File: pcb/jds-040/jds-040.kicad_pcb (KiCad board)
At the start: 2 copper layers, 18.1 x 21.5 mm, 8 parts, among them J1 USB_C_Receptacle_USB2.0, J2 Conn_01x12_MountingPin

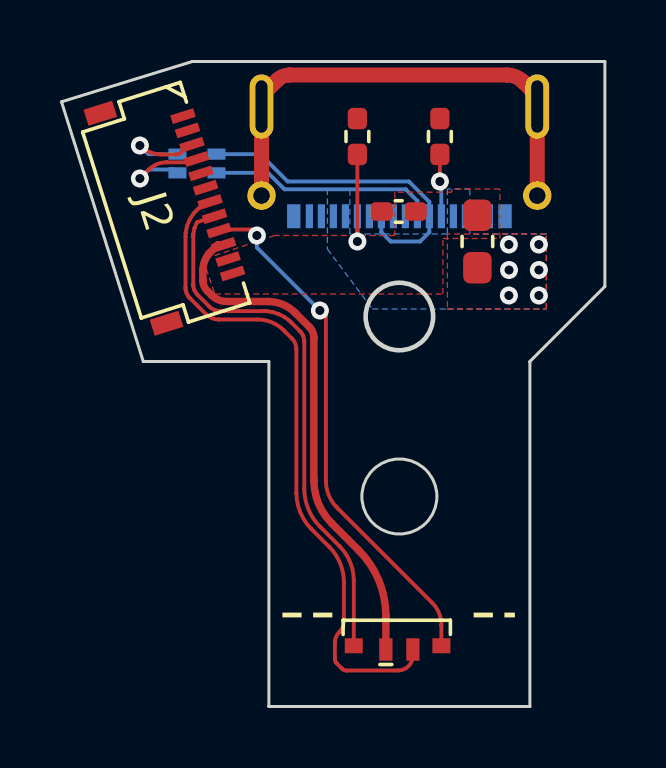
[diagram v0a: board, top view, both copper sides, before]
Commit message: Rounded all tracks, increased spaces in ground zone.
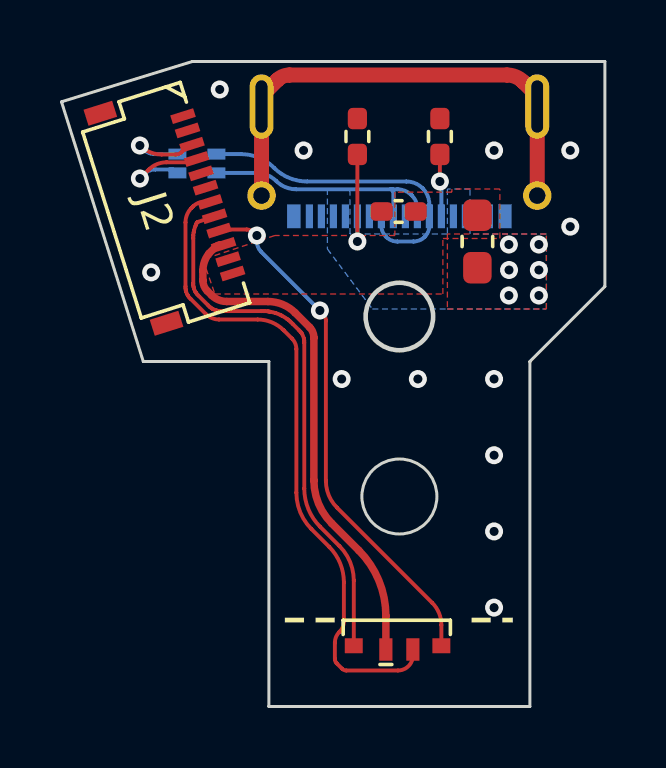
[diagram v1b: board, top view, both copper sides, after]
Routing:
- net /OD-: track 7.60 -> 8.43 mm
- net GND: vias 0 -> 12

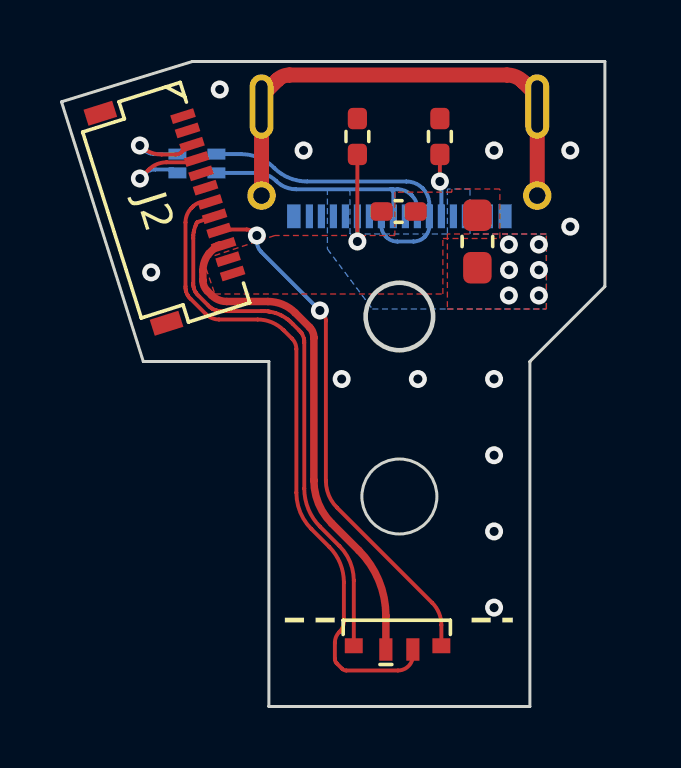
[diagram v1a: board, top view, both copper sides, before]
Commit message: Finished silkscreen, minor adjustments.
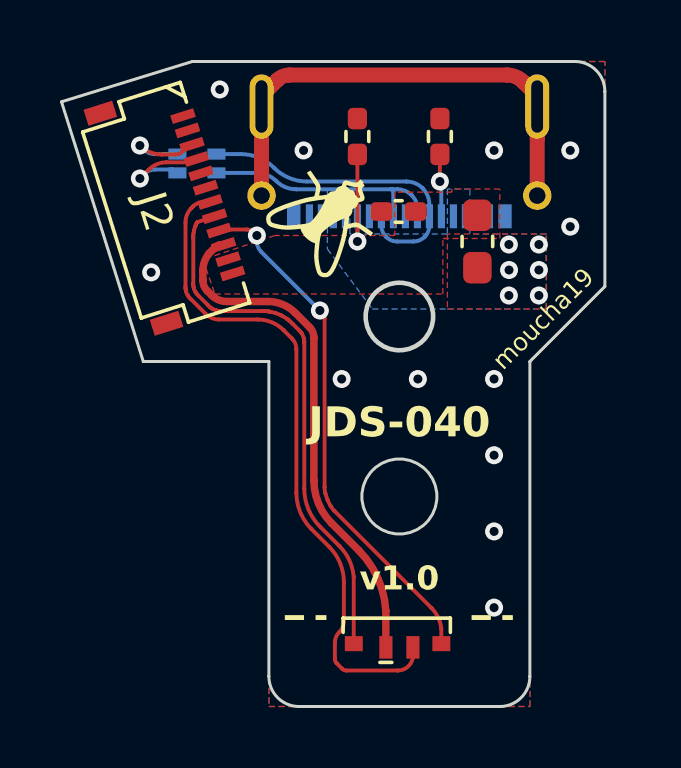
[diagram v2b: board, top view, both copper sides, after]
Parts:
- added REF**: Logo_Moucha_3x3mm_SilkScreen, Moucha_Graphics:Logo_Moucha_3x3mm_SilkScreen, F.Cu at (93.2, 95.2)
- C1: value 100nF -> 10nF
- moved D2 0.07 mm to (95.7, 109.5)
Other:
- outline, holes or cut-outs redrawn
- board text added: "JDS-040"
- board text added: "moucha19"
- board text added: "v1.0"

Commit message: Fixed DRC errors, cleaned tracks.
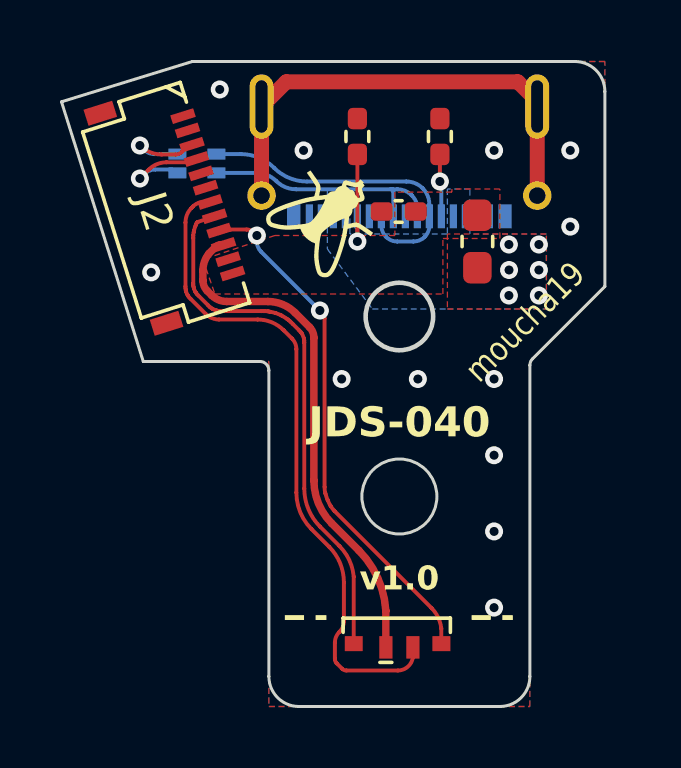
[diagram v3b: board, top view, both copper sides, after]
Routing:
- net /OD+: track 11.2 -> 10.3 mm
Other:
- outline, holes or cut-outs redrawn
- board text added: "JLCJLCJLCJLC"

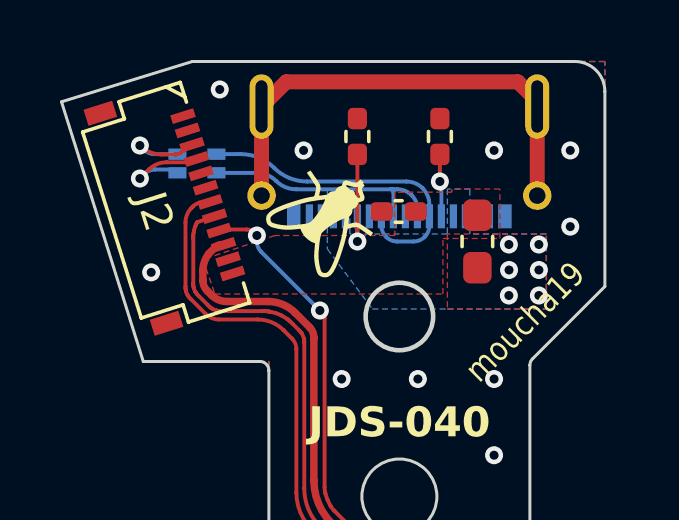
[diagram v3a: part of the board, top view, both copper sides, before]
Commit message: Increased thermal relief bridge width, minor fixes.
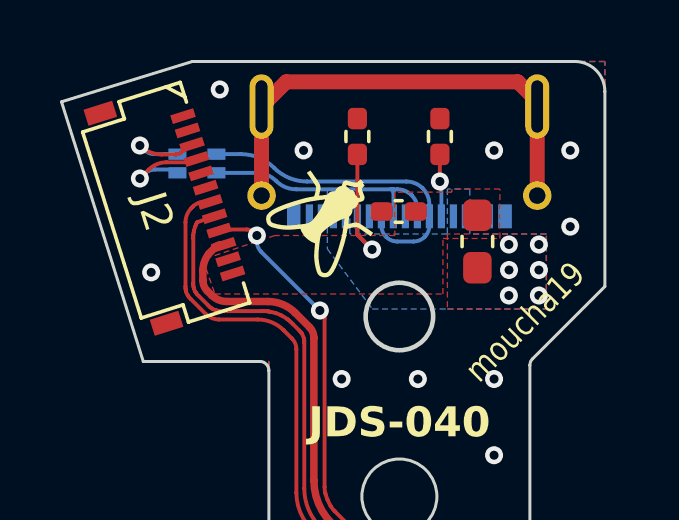
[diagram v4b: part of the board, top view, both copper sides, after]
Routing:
- net Net-(J1-CC1): track 3.74 -> 4.68 mm
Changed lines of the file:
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@@
     )
   )
-  (footprint "Moucha_Connectors:USBC_Receptacle_GT-USB-7025" (layer "B.Cu")
+  (footprint "Moucha_Connectors:USBC_Receptacle_GT-USB-7025" locked (layer "B.Cu")
     (at 95.65 91.5)
     (descr "Short USB Type-C receptacle for USB 2.0 and PD")
@@
     (property "ki_description" "USB 2.0-only Type-C Receptacle connector")
     (property "ki_keywords" "usb universal serial bus type-C USB2.0")
-    (attr smd)
+    (attr through_hole)
     (fp_text reference "J1" (at 0 0 180) (layer "B.SilkS")
         (effects (font (size 1 1) (thickness 0.15)) (justify mirror))
@@
     (fp_line (start 4.595 3.65) (end 4.595 -2.54)
       (stroke (width 0.1) (type solid)) (layer "B.Fab"))
-    (pad "A1" smd rect (at -3.52 3.66) (size 0.45 0.8) (layers "B.Cu" "B.Paste" "B.Mask")
-      (net 2 "GND") (pinfunction "GND") (pintype "passive"))
-    (pad "A1" smd rect (at -3 3.66) (size 0.24 0.8) (layers "B.Cu" "B.Paste" "B.Mask")
-      (net 2 "GND") (pinfunction "GND") (pintype "passive"))
-    (pad "A4" smd rect (at -2.2 3.66) (size 0.24 0.8) (layers "B.Cu" "B.Paste" "B.Mask")
+    (pad "A1" smd rect locked (at -3.52 3.66) (size 0.45 0.8) (layers "B.Cu" "B.Paste" "B.Mask")
+      (net 2 "GND") (pinfunction "GND") (pintype "passive"))
+    (pad "A1" smd rect locked (at -3 3.66) (size 0.24 0.8) (layers "B.Cu" "B.Paste" "B.Mask")
+      (net 2 "GND") (pinfunction "GND") (pintype "passive"))
+    (pad "A4" smd rect locked (at -2.2 3.66) (size 0.24 0.8) (layers "B.Cu" "B.Paste" "B.Mask")
       (net 1 "VBUS") (pinfunction "VBUS") (pintype "passive"))
-    (pad "A5" smd rect (at -1.4 3.66) (size 0.24 0.8) (layers "B.Cu" "B.Paste" "B.Mask")
+    (pad "A5" smd rect locked (at -1.4 3.66) (size 0.24 0.8) (layers "B.Cu" "B.Paste" "B.Mask")
       (net 12 "Net-(J1-CC1)") (pinfunction "CC1") (pintype "bidirectional"))
-    (pad "A6" smd rect (at -0.6 3.66) (size 0.24 0.8) (layers "B.Cu" "B.Paste" "B.Mask")
+    (pad "A6" smd rect locked (at -0.6 3.66) (size 0.24 0.8) (layers "B.Cu" "B.Paste" "B.Mask")
       (net 10 "/OD+") (pinfunction "D+") (pintype "bidirectional"))
-    (pad "A7" smd rect (at -0.2 3.66) (size 0.24 0.8) (layers "B.Cu" "B.Paste" "B.Mask")
+    (pad "A7" smd rect locked (at -0.2 3.66) (size 0.24 0.8) (layers "B.Cu" "B.Paste" "B.Mask")
       (net 8 "/OD-") (pinfunction "D-") (pintype "bidirectional"))
-    (pad "A8" smd rect (at 0.2 3.66) (size 0.24 0.8) (layers "B.Cu" "B.Paste" "B.Mask")
+    (pad "A8" smd rect locked (at 0.2 3.66) (size 0.24 0.8) (layers "B.Cu" "B.Paste" "B.Mask")
       (net 13 "unconnected-(J1-SBU1-PadA8)") (pinfunction "SBU1") (pintype "bidirectional+no_connect"))
-    (pad "A9" smd rect (at 1.8 3.66) (size 0.24 0.8) (layers "B.Cu" "B.Paste" "B.Mask")
+    (pad "A9" smd rect locked (at 1.8 3.66) (size 0.24 0.8) (layers "B.Cu" "B.Paste" "B.Mask")
       (net 1 "VBUS") (pinfunction "VBUS") (pintype "passive"))
-    (pad "A12" smd rect (at 2.6 3.66) (size 0.24 0.8) (layers "B.Cu" "B.Paste" "B.Mask")
-      (net 2 "GND") (pinfunction "GND") (pintype "passive"))
-    (pad "B1" smd rect (at 3 3.66) (size 0.24 0.8) (layers "B.Cu" "B.Paste" "B.Mask")
-      (net 2 "GND") (pinfunction "GND") (pintype "passive"))
-    (pad "B1" smd rect (at 3.52 3.66) (size 0.45 0.8) (layers "B.Cu" "B.Paste" "B.Mask")
-      (net 2 "GND") (pinfunction "GND") (pintype "passive"))
-    (pad "B4" smd rect (at 2.2 3.66) (size 0.24 0.8) (layers "B.Cu" "B.Paste" "B.Mask")
+    (pad "A12" smd rect locked (at 2.6 3.66) (size 0.24 0.8) (layers "B.Cu" "B.Paste" "B.Mask")
+      (net 2 "GND") (pinfunction "GND") (pintype "passive"))
+    (pad "B1" smd rect locked (at 3 3.66) (size 0.24 0.8) (layers "B.Cu" "B.Paste" "B.Mask")
+      (net 2 "GND") (pinfunction "GND") (pintype "passive"))
+    (pad "B1" smd rect locked (at 3.52 3.66) (size 0.45 0.8) (layers "B.Cu" "B.Paste" "B.Mask")
+      (net 2 "GND") (pinfunction "GND") (pintype "passive"))
+    (pad "B4" smd rect locked (at 2.2 3.66) (size 0.24 0.8) (layers "B.Cu" "B.Paste" "B.Mask")
       (net 1 "VBUS") (pinfunction "VBUS") (pintype "passive"))
-    (pad "B5" smd rect (at 1.4 3.66) (size 0.24 0.8) (layers "B.Cu" "B.Paste" "B.Mask")
+    (pad "B5" smd rect locked (at 1.4 3.66) (size 0.24 0.8) (layers "B.Cu" "B.Paste" "B.Mask")
       (net 14 "Net-(J1-CC2)") (pinfunction "CC2") (pintype "bidirectional"))
-    (pad "B6" smd rect (at 1 3.66) (size 0.24 0.8) (layers "B.Cu" "B.Paste" "B.Mask")
+    (pad "B6" smd rect locked (at 1 3.66) (size 0.24 0.8) (layers "B.Cu" "B.Paste" "B.Mask")
       (net 10 "/OD+") (pinfunction "D+") (pintype "bidirectional"))
-    (pad "B7" smd rect (at 0.6 3.66) (size 0.24 0.8) (layers "B.Cu" "B.Paste" "B.Mask")
+    (pad "B7" smd rect locked (at 0.6 3.66) (size 0.24 0.8) (layers "B.Cu" "B.Paste" "B.Mask")
       (net 8 "/OD-") (pinfunction "D-") (pintype "bidirectional"))
-    (pad "B8" smd rect (at -1 3.66) (size 0.24 0.8) (layers "B.Cu" "B.Paste" "B.Mask")
+    (pad "B8" smd rect locked (at -1 3.66) (size 0.24 0.8) (layers "B.Cu" "B.Paste" "B.Mask")
       (net 15 "unconnected-(J1-SBU2-PadB8)") (pinfunction "SBU2") (pintype "bidirectional+no_connect"))
-    (pad "B9" smd rect (at -1.8 3.66) (size 0.24 0.8) (layers "B.Cu" "B.Paste" "B.Mask")
+    (pad "B9" smd rect locked (at -1.8 3.66) (size 0.24 0.8) (layers "B.Cu" "B.Paste" "B.Mask")
       (net 1 "VBUS") (pinfunction "VBUS") (pintype "passive"))
-    (pad "B12" smd rect (at -2.6 3.66) (size 0.24 0.8) (layers "B.Cu" "B.Paste" "B.Mask")
-      (net 2 "GND") (pinfunction "GND") (pintype "passive"))
-    (pad "S1" thru_hole oval (at -4.595 0) (size 0.8 2.15) (drill oval 0.4 1.75) (layers "*.Cu" "*.Mask")
+    (pad "B12" smd rect locked (at -2.6 3.66) (size 0.24 0.8) (layers "B.Cu" "B.Paste" "B.Mask")
+      (net 2 "GND") (pinfunction "GND") (pintype "passive"))
+    (pad "S1" thru_hole oval locked (at -4.595 0) (size 0.8 2.15) (drill oval 0.4 1.75) (layers "*.Cu" "*.Mask")
       (net 16 "/SHIELD") (pinfunction "SHIELD") (pintype "passive"))
-    (pad "S1" thru_hole circle (at -4.595 2.97) (size 0.95 0.95) (drill 0.55) (layers "*.Cu" "*.Mask")
+    (pad "S1" thru_hole circle locked (at -4.595 2.97) (size 0.95 0.95) (drill 0.55) (layers "*.Cu" "*.Mask")
       (net 16 "/SHIELD") (pinfunction "SHIELD") (pintype "passive"))
-    (pad "S1" thru_hole oval (at 4.595 0) (size 0.8 2.15) (drill oval 0.4 1.75) (layers "*.Cu" "*.Mask")
+    (pad "S1" thru_hole oval locked (at 4.595 0) (size 0.8 2.15) (drill oval 0.4 1.75) (layers "*.Cu" "*.Mask")
       (net 16 "/SHIELD") (pinfunction "SHIELD") (pintype "passive"))
-    (pad "S1" thru_hole circle (at 4.595 2.97) (size 0.95 0.95) (drill 0.55) (layers "*.Cu" "*.Mask")
+    (pad "S1" thru_hole circle locked (at 4.595 2.97) (size 0.95 0.95) (drill 0.55) (layers "*.Cu" "*.Mask")
       (net 16 "/SHIELD") (pinfunction "SHIELD") (pintype "passive"))
     (model "${MOUCHA_LIB}/Moucha.3dshapes/USBC_Receptacle_TYPE-C-31-M-12.step"
@@
   (segment (start 87 92.8) (end 87.14375 92.94375) (width 0.13) (layer "B.Cu") (net 11))
   (arc (start 87.490793 93.0875) (mid 87.302974 93.05014) (end 87.14375 92.94375) (width 0.13) (layer "B.Cu") (net 11))
-  (segment (start 94.25 96) (end 94.25 93.0975) (width 0.13) (layer "F.Cu") (net 12))
-  (via (at 94.25 96) (size 0.6) (drill 0.3) (layers "F.Cu" "B.Cu") (net 12))
-  (segment (start 94.25 96) (end 94.25 95.16) (width 0.13) (layer "B.Cu") (net 12))
+  (segment (start 94.25 95.774) (end 94.25 93.0975) (width 0.13) (layer "F.Cu") (net 12))
+  (segment (start 94.742 96.266) (end 94.25 95.774) (width 0.13) (layer "F.Cu") (net 12))
+  (via (at 94.742 96.266) (size 0.6) (drill 0.3) (layers "F.Cu" "B.Cu") (net 12))
+  (segment (start 94.742 96.266) (end 94.25 95.774) (width 0.13) (layer "B.Cu") (net 12))
+  (segment (start 94.25 95.774) (end 94.25 95.16) (width 0.13) (layer "B.Cu") (net 12))
   (segment (start 97 94) (end 97 93.0975) (width 0.13) (layer "F.Cu") (net 14))
   (via (at 97 94) (size 0.6) (drill 0.3) (layers "F.Cu" "B.Cu") (net 14))
@@
     (connect_pads (clearance 0.13))
     (min_thickness 0.13) (filled_areas_thickness no)
-    (fill yes (thermal_gap 0.13) (thermal_bridge_width 0.13) (smoothing fillet))
+    (fill yes (thermal_gap 0.13) (thermal_bridge_width 0.25) (smoothing fillet))
     (polygon
       (pts
@@
     (connect_pads (clearance 0.13))
     (min_thickness 0.13) (filled_areas_thickness no)
-    (fill yes (mode hatch) (thermal_gap 0.13) (thermal_bridge_width 0.13) (smoothing fillet)
+    (fill yes (mode hatch) (thermal_gap 0.13) (thermal_bridge_width 0.25) (smoothing fillet)
       (hatch_thickness 0.15) (hatch_gap 0.2) (hatch_orientation 45)
       (hatch_border_algorithm hatch_thickness) (hatch_min_hole_area 0.3))
@@
     (connect_pads (clearance 0.13))
     (min_thickness 0.13) (filled_areas_thickness no)
-    (fill yes (thermal_gap 0.13) (thermal_bridge_width 0.13) (smoothing fillet))
+    (fill yes (thermal_gap 0.13) (thermal_bridge_width 0.25) (smoothing fillet))
     (polygon
       (pts
@@
     (connect_pads (clearance 0.13))
     (min_thickness 0.13) (filled_areas_thickness no)
-    (fill yes (thermal_gap 0.13) (thermal_bridge_width 0.13) (smoothing fillet))
+    (fill yes (thermal_gap 0.13) (thermal_bridge_width 0.25) (smoothing fillet))
     (polygon
       (pts
@@
     (connect_pads (clearance 0.13))
     (min_thickness 0.13) (filled_areas_thickness no)
-    (fill yes (thermal_gap 0.13) (thermal_bridge_width 0.13) (smoothing fillet))
+    (fill yes (thermal_gap 0.13) (thermal_bridge_width 0.25) (smoothing fillet))
     (polygon
       (pts

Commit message: Updated sheets and component properties.
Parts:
- J2: value Conn_01x12_MountingPin -> FPC_01x12
- moved FL1 30.7 mm to (89.3, 62.7)
- moved J1 30.7 mm to (96.1, 60.8)
- moved R1 30.7 mm to (97.4, 61.8)
- moved R2 30.7 mm to (94.7, 61.8)
- moved C1 30.7 mm to (96.0, 64.3)
- moved D2 30.7 mm to (96.1, 78.8)
- moved F2 30.7 mm to (98.7, 65.3)
- moved J2 30.7 mm to (87.9, 64.3)
- moved REF** 30.7 mm to (93.6, 64.5)
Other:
- outline, holes or cut-outs redrawn
- board text added: "v${REVISION}"
- board text removed: "v1.0"
